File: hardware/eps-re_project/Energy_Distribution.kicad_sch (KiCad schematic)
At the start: 22 parts, among them J1 533980271, J2 533980671, J300 533980271, J302 533980671, Q1 NVTFS5116PLTAG, Q2 NVTFS5116PLTAG, Q3 NVTFS5116PLTAG, Q4 NVTFS5116PLTAG, U21 LMV321RIYLT, U300 INA199C3DCKR

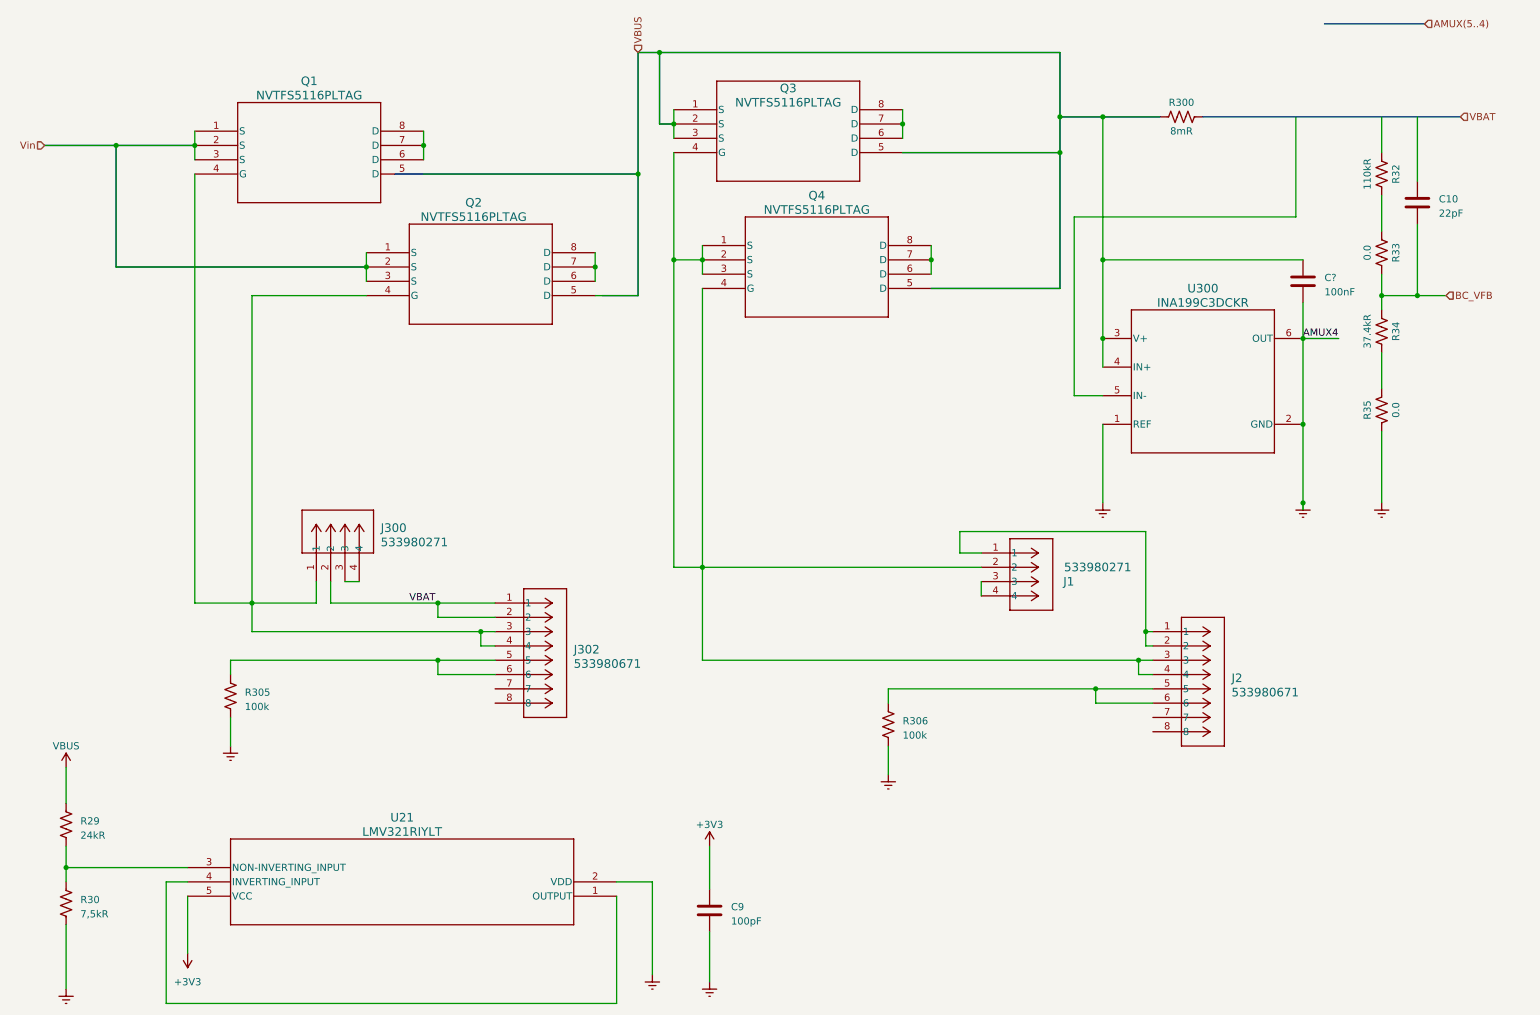
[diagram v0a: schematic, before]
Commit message: hardware: Restructuring the circuit, modifying symbols, footprints and other corrections
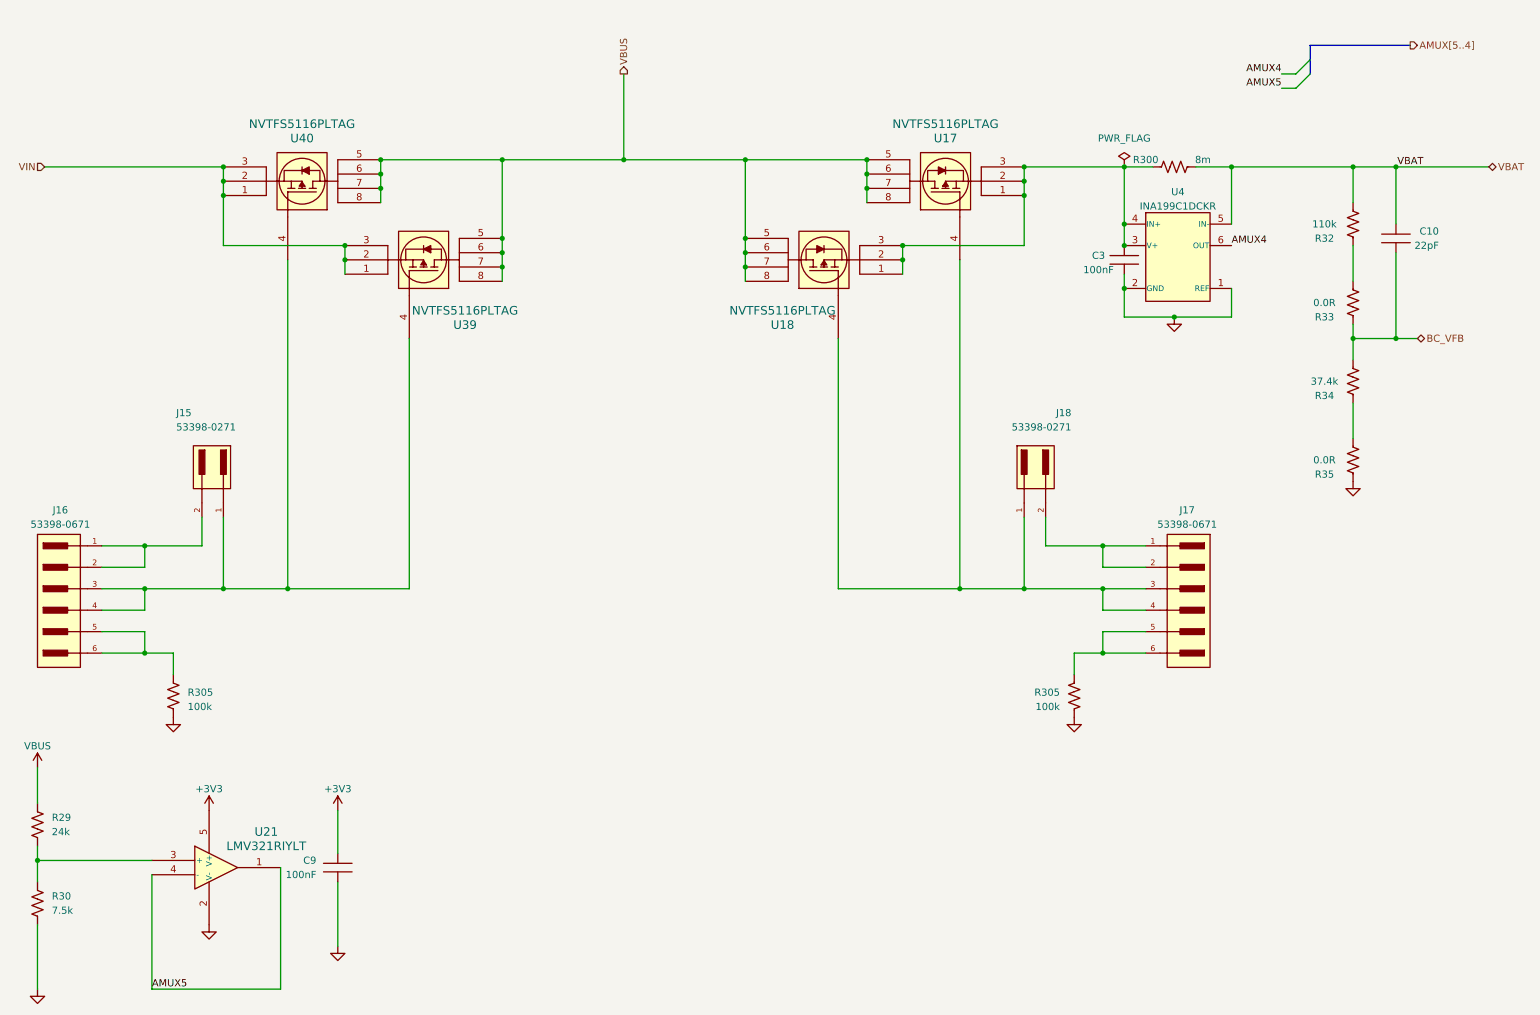
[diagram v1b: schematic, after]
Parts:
- removed C?: 100nF, symbol Device:C
- removed J1, J300: 533980271, CON_533980271, symbol 533980271:533980271
- removed J2, J302: 533980671, CON_533980671, symbol 533980671:533980671
- removed Q1, Q2, Q3, Q4: NVTFS5116PLTAG, WDFN8_3P30X3P30_ONS, symbol NVTFS5116PLTAG:NVTFS5116PLTAG
- removed R306: 100k, symbol Device:R_US
- removed U300: INA199C3DCKR, DCK0006A_N, symbol INA199C3DCKR:INA199C3DCKR
- added C3: 100nF, footprints:C0603C104K5RACTU, symbol C0603C104K5RACTU:C0603C104K5RACTU
- added J15, J18: 53398-0271, footprints:533980271, symbol 533980271:53398-0271
- added J16, J17: 53398-0671, footprints:533980671, symbol 533980671:53398-0671
- added R305: 100k, symbol Device:R_US
- added U17, U18, U39, U40: NVTFS5116PLTAG, footprints:NVTFS5116PLTAG, symbol NVTFS5116PLWFTAG:NVTFS5116PLTAG
- added U4: INA199C1DCKR, footprints:INA199C1DCKR, symbol INA199C1DCKR:INA199xxDCK
- C10: footprint (none) -> footprints:C0603C220K5RACAUTO; symbol Device:C -> C0603C220K5RACAUTO:C0603C220K5RACAUTO; automotive (none) -> Yes; automotive grade (none) -> Grade 1; capacitance (none) -> 22 pF; category (none) -> Cap; device class L1 (none) -> Passive Components; device class L2 (none) -> Capacitors; device class L3 (none) -> Ceramic Capacitors; digikey description (none) -> Cap Ceramic 22pF 50V X7R 10% SMD 0603 125°C Punched Paper T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; digikey part number (none) -> 399-13715-2-ND; height (none) -> 0.87mm; lead free (none) -> Yes; library id (none) -> f369d16140aeee74; manufacturer (none) -> KEMET; material (none) -> Ceramic; mouser description (none) -> Cap Ceramic 22pF 50V X7R 10% SMD 0603 125°C Punched Paper T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; mouser part number (none) -> 80-C0603C220K5RAUTO; package (none) -> 0603; rohs (none) -> Yes; temperature characteristic (none) -> X7R; temperature coefficient (none) -> 30ppm/°C; temperature range high (none) -> +125°C; temperature range low (none) -> -55°C; tolerance (none) -> 0.1; voltage rating (none) -> 50 V
- C9: value 100pF -> 100nF; footprint (none) -> footprints:C0603C104K5RACTU; symbol Device:C -> C0603C104K5RACTU:C0603C104K5RACTU; automotive (none) -> Yes; automotive grade (none) -> Grade 1; capacitance (none) -> 0.10 μF; category (none) -> Cap; device class L1 (none) -> Passive Components; device class L2 (none) -> Capacitors; device class L3 (none) -> Ceramic Capacitors; digikey description (none) -> CAP CER 0.1UF 50V X7R 0603; digikey part number (none) -> 399-5089-2-ND; height (none) -> 0.87mm; lead free (none) -> Yes; library id (none) -> 73022d3323b2b2b8; manufacturer (none) -> KEMET; material (none) -> Ceramic; mouser part number (none) -> 80-C0603C104K5R7867; package (none) -> 0603; rohs (none) -> Yes; temperature characteristic (none) -> X7R; temperature coefficient (none) -> 30ppm/°C; temperature range high (none) -> +125°C; temperature range low (none) -> -55°C; tolerance (none) -> 0.1; voltage rating (none) -> 50 V
- R29: value 24kR -> 24k
- R30: value 7,5kR -> 7.5k
- R300: value 8mR -> 8m
- R32: value 110kR -> 110k
- R33, R35: value 0.0 -> 0.0R
- R34: value 37.4kR -> 37.4k
- U21: footprint SOT23-5_STM -> footprints:LMV321RIYLT
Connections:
- net VBAT: now also C10.1, R300.2, R32.1, U4.5 (IN-)
- net VBUS: now also U17.5, U17.6, U17.7, U17.8, U18.5, U18.6, U18.7, U18.8, U39.5, U39.6, U39.7, U39.8, U40.5, U40.6, U40.7, U40.8; no longer R300.1
- net at R305.1: now also J16.5, J16.6
- net AMUX5: now reaches U21.1, U21.4 (-)
- net Earth renamed GND
- net GND: now also C3.2, R305.2, U4.1 (REF), U4.2 (GND)
- new net: C3.1, R300.1, U17.1, U17.2, U17.3, U18.1, U18.2, U18.3, U4.3 (V+), U4.4 (IN+)
- new net: J17.3, J17.4, J18.1, U17.4, U18.4
- new net: J15.1, J16.3, J16.4, U39.4, U40.4
- new net: J17.1, J17.2, J18.2
- new net: J17.5, J17.6, R305.1
- new net: J15.2, J16.1, J16.2
- new net AMUX4: U4.6 (OUT)
- new net VIN: U39.1, U39.2, U39.3, U40.1, U40.2, U40.3
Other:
- moved on the sheet: C10, C9, R29, R30, R305, R32, R33, R34, R35
